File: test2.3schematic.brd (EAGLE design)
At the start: 16.4 x 22.3 mm, 24 parts, among them IC1 NCS21911SN2T1G, IC2 FXLN8371QR1, IC3 MAX25210ATAB9_V+, IC4 NCS21911SN2T1G, IC5 NCS21911SN2T1G

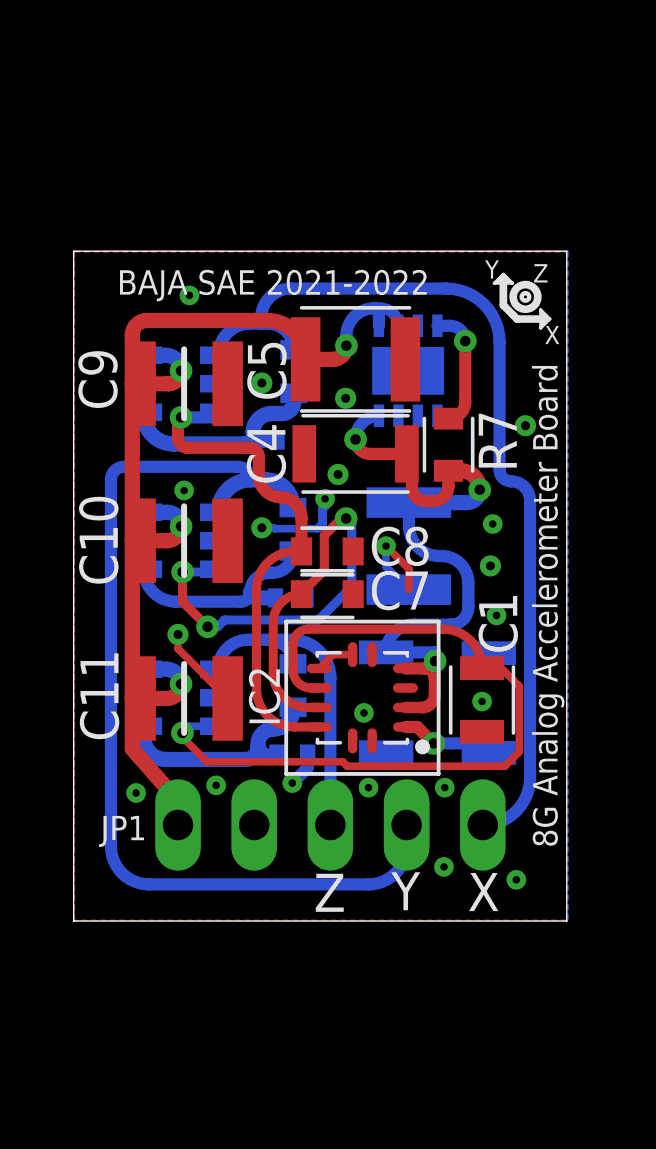
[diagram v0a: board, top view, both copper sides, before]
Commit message: No Errors on the board waiting for Forrest to confirm and explain what pin 9 EP is
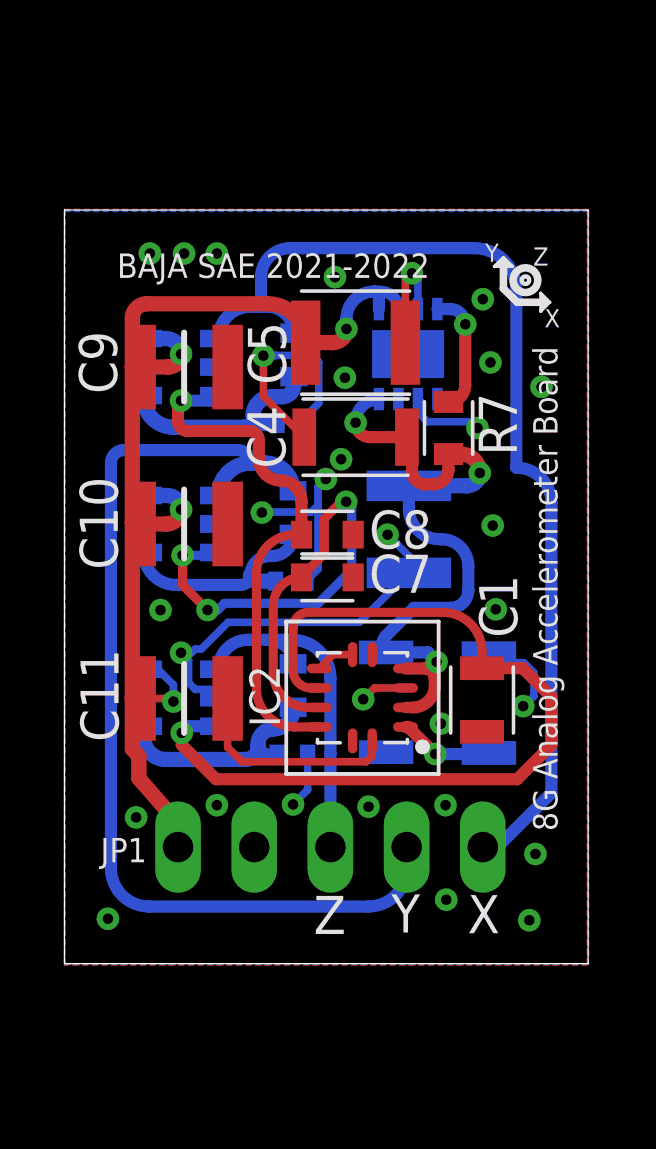
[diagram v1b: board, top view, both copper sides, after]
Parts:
- moved JP1 0.74 mm to (7.87, 1.80)
- moved C2 0.56 mm to (10.5, 12.4)
- moved C5 0.56 mm to (8.71, 18.6)
- moved IC3 0.56 mm to (10.5, 18.2)
- moved R6 0.56 mm to (6.65, 18.2)
- moved C10 0.56 mm to (3.00, 12.6)
- moved C4 0.56 mm to (8.71, 15.5)
- moved C7 0.56 mm to (7.77, 10.8)
- moved C8 0.56 mm to (7.77, 12.2)
- moved IC4 0.56 mm to (2.90, 12.6)
- moved R2 0.56 mm to (6.60, 15.9)
- moved R3 0.56 mm to (6.55, 10.7)
- moved R5 0.56 mm to (6.63, 13.0)
- moved R7 0.56 mm to (11.8, 15.8)
- moved C9 0.56 mm to (3.00, 17.8)
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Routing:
- net GND: track 12.1 -> 47.0 mm, vias 22 -> 31
- net X_OUT: track 29.8 -> 34.1 mm
- net Z_AXIS: track 26.0 -> 29.4 mm
- net Y_OUT: track 32.2 -> 33.5 mm
- net V_12V: track 38.2 -> 39.3 mm
- net Z_OUT: track 10.7 -> 11.4 mm
- net X_AXIS: track 16.7 -> 17.3 mm
- net Y_AXIS: track 19.4 -> 19.9 mm
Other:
- board size 16.4 x 22.3 mm -> 17.5 x 25.1 mm

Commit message: NO errors Everything done and connected, PCB Design has been completed now waiting for Forrest's Review, if HE approves then done if not this is just a draft
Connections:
- net GND: now also IC3.9
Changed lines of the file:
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@@
 <drawing>
 <settings>
-<setting alwaysvectorfont="yes"/>
+<setting alwaysvectorfont="no"/>
 <setting verticaltext="up"/>
 </settings>
@@
 <wire x1="4.9276" y1="4.6482" x2="4.4472" y2="5.1286" width="0.254" layer="1"/>
 <wire x1="4.4472" y1="5.1286" x2="4.4472" y2="6.7564" width="0.254" layer="1"/>
+<contactref element="IC3" pad="9"/>
 </signal>
 <signal name="BYP">

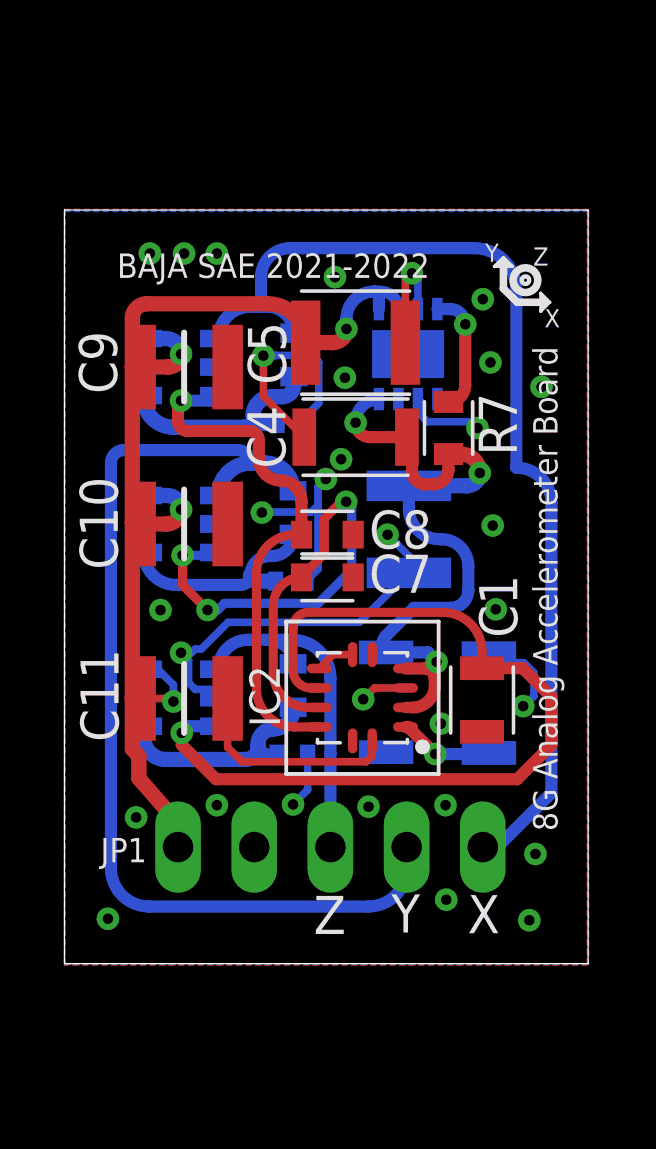
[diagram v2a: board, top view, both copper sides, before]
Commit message: FInal PCB, some parts might be bought using diff website if not PCB will be revised for later deadline
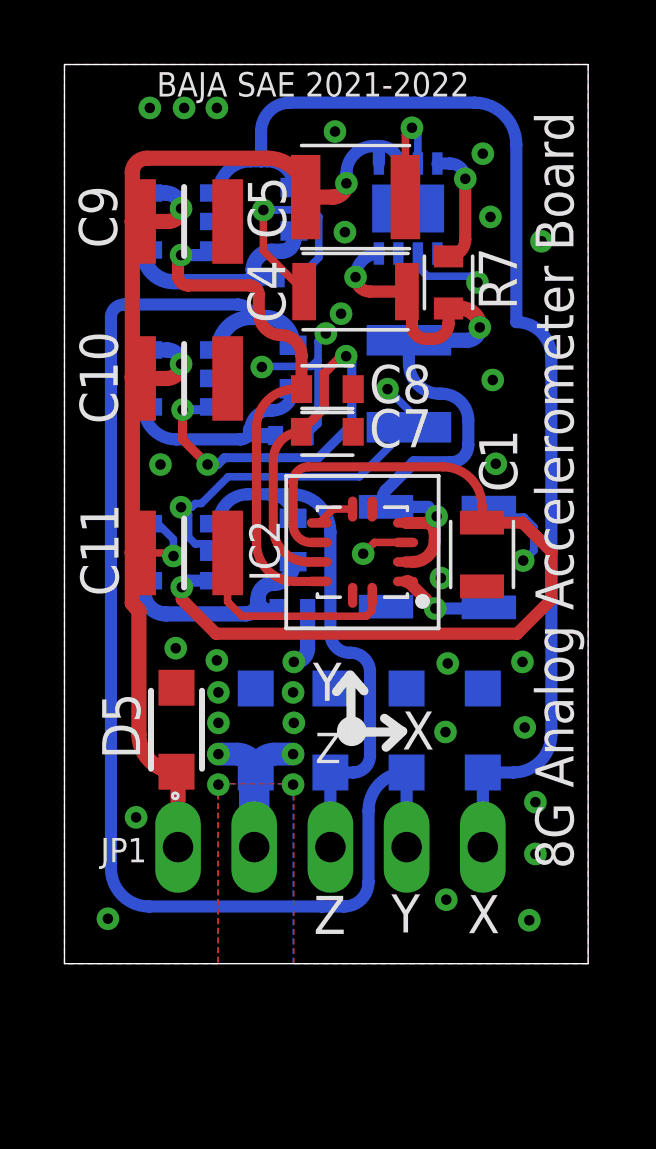
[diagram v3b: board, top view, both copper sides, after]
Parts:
- added D1, D2, D3, D4, D5: PTVS12VS1UR,115, SamacSys_Parts:SOD123W
- moved C9 4.85 mm to (3.00, 22.7)
- moved IC1 4.85 mm to (2.90, 22.7)
- moved C1 4.85 mm to (12.9, 11.6)
- moved IC2 4.85 mm to (8.94, 11.6)
- moved IC5 4.85 mm to (2.90, 11.6)
- moved R4 4.85 mm to (6.60, 9.75)
- moved C2 4.85 mm to (10.5, 17.2)
- moved C3 4.85 mm to (9.73, 11.5)
- moved C4 4.85 mm to (8.71, 20.3)
- moved C7 4.85 mm to (7.77, 15.6)
- moved C8 4.85 mm to (7.77, 17.1)
- moved R1 4.85 mm to (6.63, 12.0)
- moved R2 4.85 mm to (6.60, 20.8)
- moved R3 4.85 mm to (6.55, 15.5)
- moved R7 4.85 mm to (11.8, 20.6)
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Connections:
- net GND: now also D1.2, D2.2, D3.2, D4.1, D4.2, D5.2
- net V_12V: now also D5.1
- net X_OUT: now also D1.1
- net Y_OUT: now also D2.1
- net Z_OUT: now also D3.1
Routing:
- net Y_OUT: track 33.5 -> 42.8 mm
- net Z_OUT: track 11.4 -> 17.9 mm
- net GND: track 47.0 -> 52.6 mm, vias 31 -> 43
- net X_OUT: track 34.1 -> 39.2 mm
- net V_12V: track 39.3 -> 44.3 mm
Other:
- board size 17.5 x 25.1 mm -> 17.5 x 30 mm
- board text added: "Designed By Kevin Foyet"
- board text removed: "Kevin Foyet"
